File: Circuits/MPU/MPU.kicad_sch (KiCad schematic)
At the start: 12 parts, among them J1 5-1814400-1, J10 Conn_02x10_Odd_Even, J11 Conn_02x04_Odd_Even, J2 5-1814400-1, J3 DE9_Plug, J4 DE9_Plug, J5 DE9_Receptacle, J6 DE9_Receptacle, J7 Conn_02x13_Odd_Even, J8 Conn_02x25_Odd_Even, J9 Conn_02x05_Odd_Even

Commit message: more transcription
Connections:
- net Power/+3.3raw renamed Power/+28V
- net Power/+5raw: no longer names the net of J11.4 (Pin_4), J11.5 (Pin_5)
- net Power/-5raw renamed Power/+28return
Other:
- sheet Power ports: added +28V, +28return; removed +3.3raw, +5raw, -5raw
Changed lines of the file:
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@@
 	)
 	(junction
-		(at 128.27 163.83)
-		(diameter 0)
-		(color 0 0 0 0)
-	)
-	(junction
 		(at 214.63 115.57)
 		(diameter 0)
@@
 	(wire
 		(pts
-			(xy 128.27 163.83) (xy 134.62 163.83)
-		)
-		(stroke
-			(width 0)
-			(type default)
-		)
-	)
-	(wire
-		(pts
 			(xy 248.92 121.92) (xy 254 121.92)
 		)
@@
 			)
 		)
-		(pin "+3.3raw" input
-			(at 134.62 161.29 180)
-			(effects
-				(font
-					(size 1.27 1.27)
-				)
-				(justify left)
-			)
-		)
-		(pin "+5raw" input
-			(at 134.62 163.83 180)
+		(pin "+28return" input
+			(at 134.62 166.37 180)
 			(effects
 				(font
@@
 			)
 		)
-		(pin "-5raw" input
-			(at 134.62 166.37 180)
+		(pin "+28V" input
+			(at 134.62 161.29 180)
 			(effects
 				(font

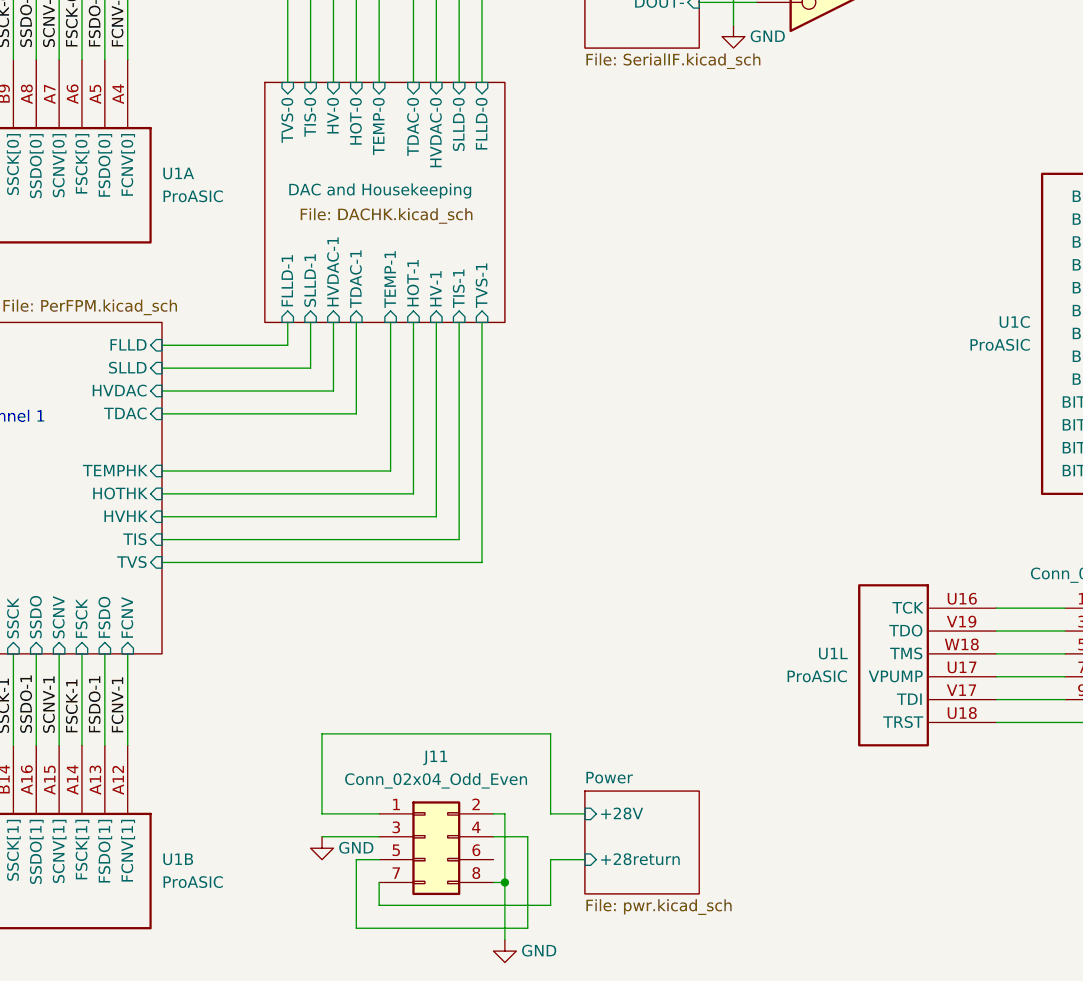
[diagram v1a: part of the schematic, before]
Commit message: All pages populated with parts
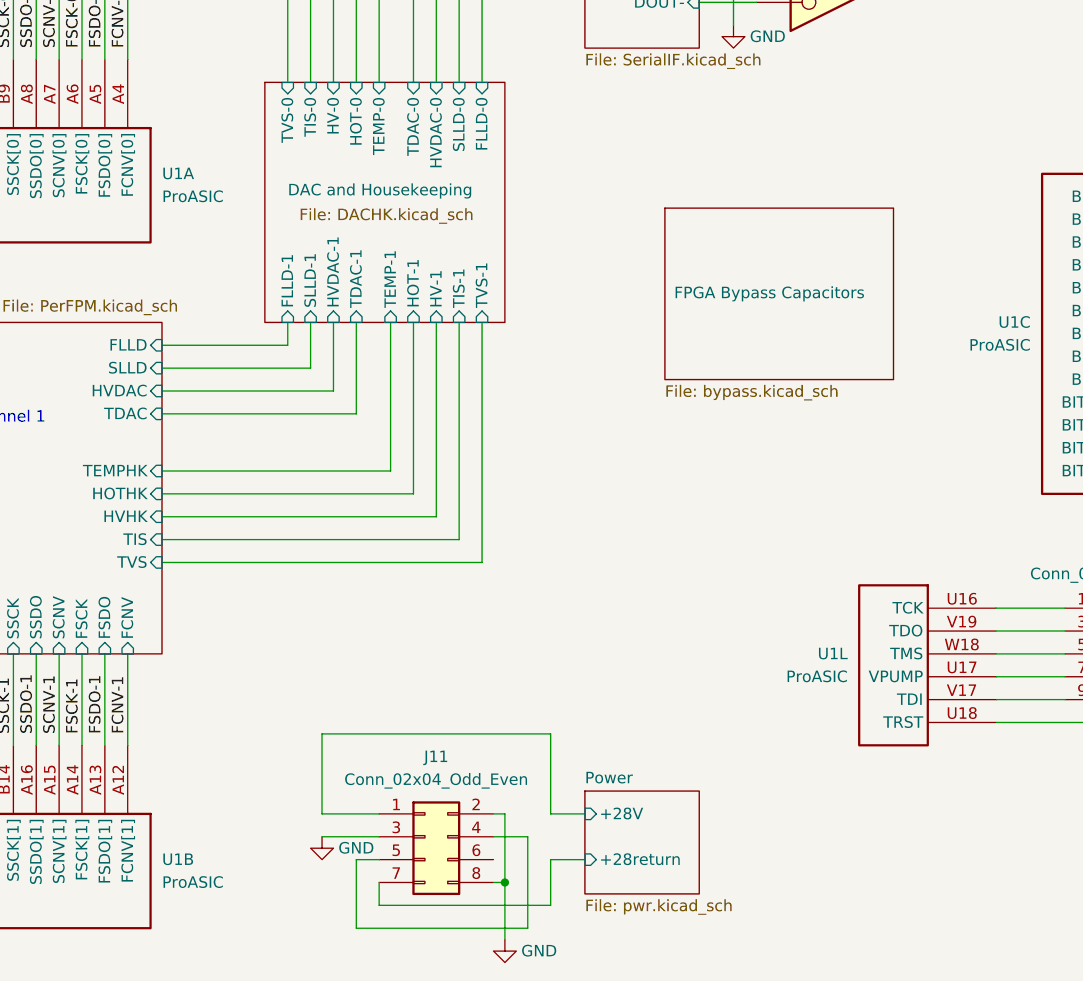
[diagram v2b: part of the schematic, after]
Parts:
- U1: renamed from 	U1
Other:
- added sheet FPGA Bypass Capacitors (bypass.kicad_sch)
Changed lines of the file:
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@@
 		(dnp no)
 		(fields_autoplaced yes)
-		(property "Reference" "	U1"
-			(at 87.63 90.17 90)
+		(property "Reference" "U1"
+			(at 87.63 90.1699 90)
 			(effects
 				(font
@@
 		)
 		(property "Value" "ProASIC"
-			(at 87.63 92.71 90)
+			(at 87.63 92.7099 90)
 			(effects
 				(font
@@
 			(project "MPU"
 				(path "/a3d8c1ad-4320-4fce-bd93-27782a1083f9"
-					(reference "	U1")
+					(reference "U1")
 					(unit 1)
 				)
@@
 		(dnp no)
 		(fields_autoplaced yes)
-		(property "Reference" "	U1"
-			(at 87.63 166.37 90)
+		(property "Reference" "U1"
+			(at 87.63 166.3699 90)
 			(effects
 				(font
@@
 		)
 		(property "Value" "ProASIC"
-			(at 87.63 168.91 90)
+			(at 87.63 168.9099 90)
 			(effects
 				(font
@@
 			(project "MPU"
 				(path "/a3d8c1ad-4320-4fce-bd93-27782a1083f9"
-					(reference "	U1")
+					(reference "U1")
 					(unit 2)
 				)
@@
 				)
 			)
+		)
+	)
+	(sheet
+		(at 143.51 93.98)
+		(size 25.4 19.05)
+		(stroke
+			(width 0.1524)
+			(type solid)
+		)
+		(fill
+			(color 0 0 0 0.0000)
+		)
+		(property "Sheetname" "FPGA Bypass Capacitors"
+			(at 144.526 104.14 0)
+			(effects
+				(font
+					(size 1.27 1.27)
+				)
+				(justify left bottom)
+			)
+		)
+		(property "Sheetfile" "bypass.kicad_sch"
+			(at 143.51 113.6146 0)
+			(effects
+				(font
+					(size 1.27 1.27)
+				)
+				(justify left top)
+			)
+		)
+		(instances
+			(project "MPU"
+				(path "/a3d8c1ad-4320-4fce-bd93-27782a1083f9"
+					(page "16")
+				)
+			)

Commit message: Passes DRC
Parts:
- removed unit 12 of 	U1
- removed unit 7 of 	U1
- added unit 13 of U1
- added unit 8 of U1
- J1, J2: Description_1 (none) -> CONN SMA JACK R/A 50 OHM PCB
- U1: manf# A3PE3000-FGG484 -> (none)
- U1: renamed from 	U1
- renumbered J8 to J11, J11 to J5, J5 to J6, J6 to J7, J9 to J8, J7 to J9
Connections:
- net LEDs/BLUE: now also U1.L1 (BLUE)
- net LEDs/GREEN: now also U1.M2 (GREEN)
- net LEDs/RED: now also U1.N2 (RED)
- net LEDs/YELLOW: now also U1.N1 (YELLOW)
- net at J8.1 (Pin_1): now also U1.U16 (TCK)
- net at J8.3 (Pin_3): now also U1.V19 (TDO)
- net at J8.5 (Pin_5): now also U1.W18 (TMS)
- net at J8.7 (Pin_7): now also U1.U17 (VPUMP)
- net at J8.8 (Pin_8): now also U1.U18 (TRST)
- net at J8.9 (Pin_9): now also U1.V17 (TDI)
- net at J10.10 (Pin_10): now also U1.U1 (DB7)
- net at J10.11 (Pin_11): now also U1.T3 (DB8)
- net at J10.12 (Pin_12): now also U1.T2 (DB9)
- net at J10.13 (Pin_13): now also U1.T1 (DB10)
- net at J10.14 (Pin_14): now also U1.R2 (DB11)
- net at J10.15 (Pin_15): now also U1.R1 (DB12)
- net at J10.16 (Pin_16): now also U1.P3 (DB13)
- net at J10.17 (Pin_17): now also U1.P2 (DB14)
- net at J10.18 (Pin_18): now also U1.P1 (DB15)
- net at J10.3 (Pin_3): now also U1.Y2 (DB0)
- net at J10.4 (Pin_4): now also U1.W2 (DB1)
- net at J10.5 (Pin_5): now also U1.W1 (DB2)
- net at J10.6 (Pin_6): now also U1.V2 (DB3)
- net at J10.7 (Pin_7): now also U1.V1 (DB4)
- net at J10.8 (Pin_8): now also U1.U3 (DB5)
- net at J10.9 (Pin_9): now also U1.U2 (DB6)
- net PerFPM/In renamed PerFPM/Pulse
- net PerFPM1/In renamed PerFPM1/Pulse
- no-connect marks 0 -> 4
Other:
- sheet PerFPM ports: added Pulse; removed HOTHK, In, TEMPHK, TVS
- sheet PerFPM1 ports: added Pulse; removed HOTHK, In, TEMPHK, TVS

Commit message: bunch of little fixes
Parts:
- removed J5: Conn_02x04_Odd_Even, symbol Connector_Generic:Conn_02x04_Odd_Even
- added J5: 0010085031, symbol Connector_Generic:Conn_01x03
- J10: footprint (none) -> Connector_PinHeader_2.54mm:PinHeader_2x10_P2.54mm_Vertical
- J11: footprint (none) -> Connector_PinHeader_2.54mm:PinHeader_2x25_P2.54mm_Vertical
- J8: footprint (none) -> Connector_PinHeader_2.54mm:PinHeader_2x05_P2.54mm_Vertical
- J9: footprint (none) -> Connector_PinHeader_2.54mm:PinHeader_2x13_P2.54mm_Vertical
- U1: footprint Package_BGA:BGA-484_23.0x23.0mm_Layout22x22_P1.0mm -> Package_BGA:BGA-484_23.0x23.0mm_Layout22x22_P1.0mm
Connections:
- net Power/+28V: now also J5.2 (Pin_2)
- net Power/+28return: now also J5.1 (Pin_1), J5.3 (Pin_3)
- no-connect marks 4 -> 3

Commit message: Better names
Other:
- sheet FPGA Bypass Capacitors renamed FPGA Power
- sheet PerFPM renamed PerFPM-0
- sheet PerFPM1 renamed PerFPM-1
- sheet SerialIF renamed Serial Interfaces
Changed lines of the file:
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@@
 			(color 0 0 0 0.0000)
 		)
-		(property "Sheetname" "PerFPM1"
+		(property "Sheetname" "PerFPM-1"
 			(at 50.8 105.9684 0)
 			(effects
@@
 			(color 0 0 0 0.0000)
 		)
-		(property "Sheetname" "SerialIF"
+		(property "Sheetname" "Serial Interfaces"
 			(at 134.62 15.7984 0)
 			(effects
@@
 			(color 0 0 0 0.0000)
 		)
-		(property "Sheetname" "FPGA Bypass Capacitors"
-			(at 144.526 104.14 0)
+		(property "Sheetname" "FPGA Power"
+			(at 150.622 104.14 0)
 			(effects
 				(font
@@
 			(color 0 0 0 0.0000)
 		)
-		(property "Sheetname" "PerFPM"
+		(property "Sheetname" "PerFPM-0"
 			(at 50.8 29.7684 0)
 			(effects
